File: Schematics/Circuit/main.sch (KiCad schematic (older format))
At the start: 101 parts, among them IC1 NCP1117ST33T3G, IC2 NCP1117ST50T3G, IC3 ATMEGA2560-A, IC4 RFM69HW, J1 Conn_01x03, J10 Conn_01x04, J11 Conn_01x04, J12 Conn_01x01, J13 Conn_01x02, J14 Conn_01x02, J15 Conn_01x02, J16 Conn_01x02, J2 Conn_01x07, J3 Conn_01x07, J4 Conn_01x07, J5 Conn_01x07, J6 Conn_01x07, J7 Conn_01x05, J8 Conn_02x05_Counter_Clockwise, J9 Conn_01x06, K1 HESOP1, K2 HESOP1, P1 CONN_2, P10 CONN_2, P11 CONN_2, P12 CONN_2, P13 CONN_2, P14 CONN_2, P15 CONN_2, P16 CONN_2, P17 CONN_2, P18 CONN_3X2, P19 CONN_O2, P2 CONN_2, P20 CONN_2, P21 CONN_2, P3 CONN_2, P4 CONN_2, P5 CONN_2, P6 CONN_2, P7 CONN_2, P8 CONN_2, P9 CONN_2, Q1 BSS138, Q2 BSS138, Q3 BSS138, Q4 BSS138, Q5 BSS138, Q6 BSS138, SW1 SW_DIP_x01, SW7 SW_DIP_x01

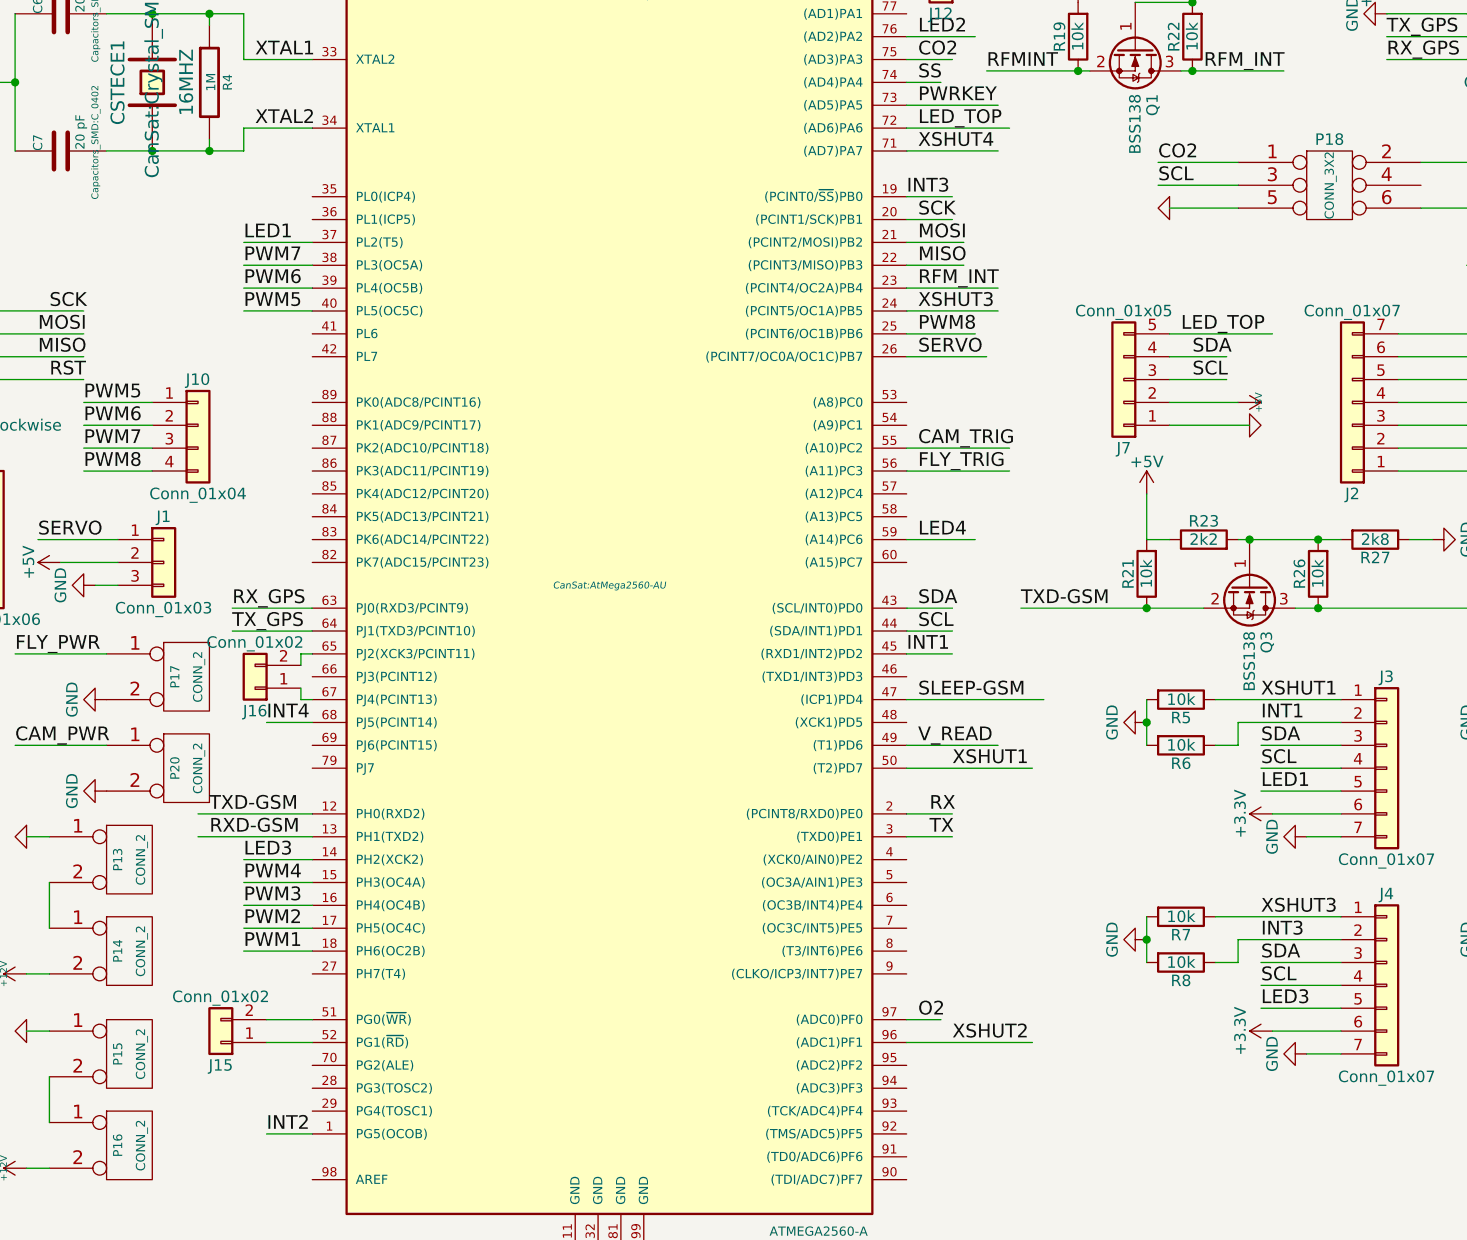
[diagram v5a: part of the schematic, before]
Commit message: Add UV and Gamma detection, fix main pcb
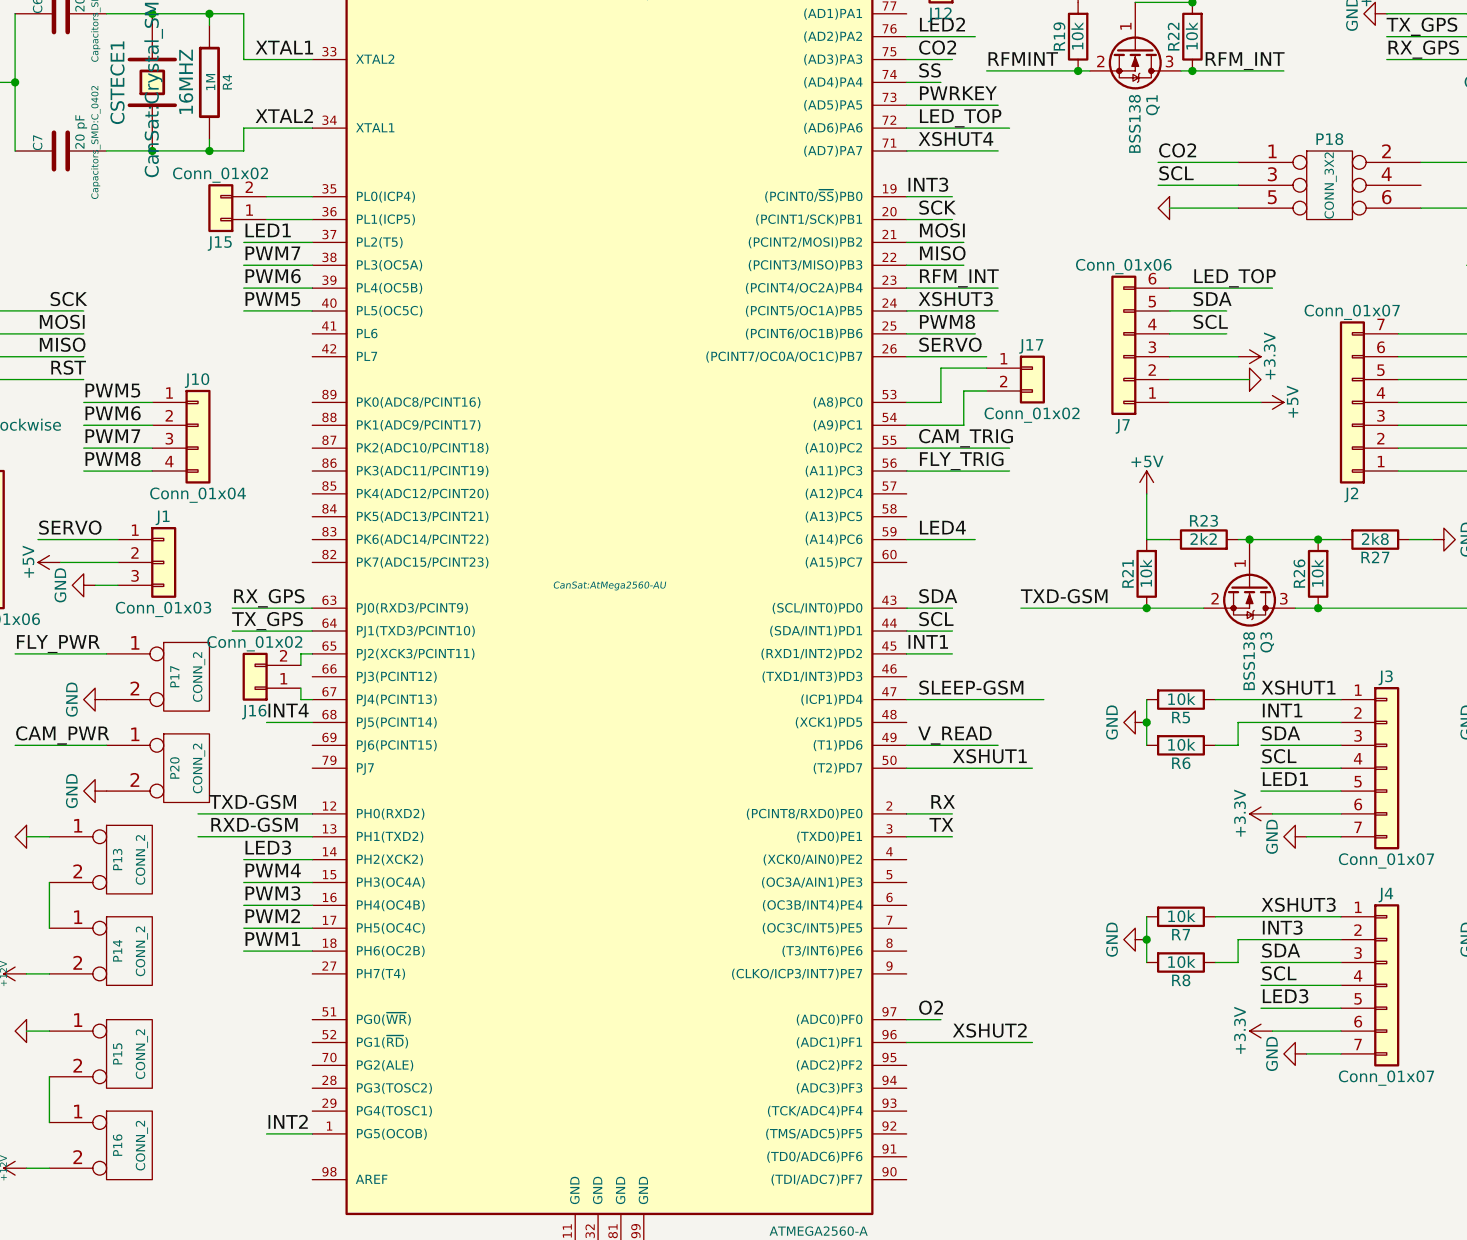
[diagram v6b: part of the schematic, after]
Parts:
- removed J7: Conn_01x05, Pin_Headers:Pin_Header_Straight_1x05_Pitch1.27mm_SMD_Pin1Right, symbol Conn_01x05
- added J17: Conn_01x02, CanSat:MOLEX_PicoBlade_2, symbol Conn_01x02
- added J7: Conn_01x06, Pin_Headers:Pin_Header_Straight_1x06_Pitch1.27mm_SMD_Pin1Left, symbol Conn_01x06
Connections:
- wire segments 277 -> 284
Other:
- moved on the sheet: J15
